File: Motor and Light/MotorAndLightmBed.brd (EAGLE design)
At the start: 100 x 110.5 mm, 136 parts, among them J6 6_PIN_SERIAL_CABLEPTH, Q1 BSS84, Q3 BC846ASMD, Q4 220mA/50V/3.5Ω, Q5 220mA/50V/3.5Ω, Q6 220mA/50V/3.5Ω, Q7 220mA/50V/3.5Ω, U1 9DoF IMU, U2 LPC1768FBD100, X1 2510-, X2 2510-, X3 C-GRID-05-15-91, X4 C-GRID-05-15-91, X5 C-GRID-02-70553, X6 SI-50170, Y1 32.768kHz, Y2 OSCILLATORSMD-5X3-50MHz, Y3 OSCILLATORSMD-5X3-12MHz

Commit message: Updated Board Design
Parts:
- removed U$3: V_REG_LD1117VXX, SparkFun-IC-Power:78XXL
- added CR1: LD1117S33TR, LD1117:SOT-223
- moved R32 194.9 mm to (79.5, 6.50), turned to 270 degrees
- moved J6 177.3 mm to (83.0, 24.5)
- moved R33 123.5 mm to (82.5, 21.0)
- moved C3 123.4 mm to (43.5, 49.0), turned to 270 degrees
- moved R54 122.1 mm to (59.5, 50.0)
- moved C10 116.2 mm to (11.0, 43.0), turned to 180 degrees
- moved Y2 114.9 mm to (47.6, 5.47)
- moved R31 112.0 mm to (11.0, 47.5)
- moved R30 109.6 mm to (11.0, 45.0)
- moved R1 104.5 mm to (8.18, 39.4)
- moved R53 102.5 mm to (48.0, 65.0)
- moved Y3 97.6 mm to (37.5, 49.0)
- moved R56 94.7 mm to (29.5, 68.5)
- moved R52 75.1 mm to (16.0, 53.8), turned to 90 degrees
- moved R51 69.8 mm to (16.0, 57.6), turned to 90 degrees
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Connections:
- new net USB_D+: C10.1, R1.2, R30.2, U2.29
- new net USB_D-: C11.1, R31.2, U2.30
- net +3V3: now also CR1.2; no longer U$3.GND
- net +5V: now also CR1.3; no longer U$3.OUT
- net GND: now also CR1.1; no longer U$3.IN
- net LEA3: now also U2.52; no longer U2.77
- net LPC_D+: no longer C10.1, R1.2, R30.2, U2.29
- net LPC_D-: no longer C11.1, R31.2, U2.30
- net REA3: now also U2.51; no longer U2.79
- net REB3: now also U2.77; no longer U2.78
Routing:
- net +3V3: track 89.9 -> 410.1 mm, vias 4 -> 19
- net +5V: track 49.9 -> 177.7 mm, vias 3 -> 6
- net GND: track 160.4 -> 270.0 mm, vias 7 -> 19
- net +12V: track 0.00 -> 91.6 mm, vias 0 -> 1
- net LED_LINK: track 0.00 -> 82.0 mm, vias 0 -> 2
- net TGT_RXD: track 0.00 -> 75.7 mm, vias 0 -> 1
- net LED_SPEED: track 0.00 -> 75.6 mm, vias 0 -> 2
- net ETH_RST: track 0.00 -> 75.4 mm, vias 0 -> 2
- net 50MHZ: track 0.00 -> 74.4 mm, vias 0 -> 6
- net TGT_TXD: track 0.00 -> 73.2 mm, vias 0 -> 1
- net VDDA: track 0.00 -> 61.5 mm, vias 0 -> 2
- net N$11: track 0.00 -> 57.6 mm, vias 0 -> 4
- net TGT_SCON: track 0.00 -> 56.5 mm, vias 0 -> 2
- net TGT_P1.17: track 0.00 -> 53.1 mm, vias 0 -> 2
- net TGT_P1.16: track 0.00 -> 50.5 mm, vias 0 -> 2
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- added copper zone on layer 16, net GND
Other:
- board size 100 x 110.5 mm -> 100 x 80 mm

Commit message: First Version of Board file
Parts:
- moved R55 124.8 mm to (65.3, 72.5)
- moved C1 122.5 mm to (50.0, 48.5), turned to 180 degrees
- moved C2 119.9 mm to (43.5, 48.5)
- moved C28 118.6 mm to (28.5, 26.5), turned to 180 degrees
- moved R29 116.7 mm to (22.5, 44.5)
- moved C26 115.1 mm to (32.0, 26.5)
- moved R57 113.6 mm to (46.2, 72.5)
- moved C29 104.4 mm to (13.1, 34.8), turned to 90 degrees
- moved Y1 93.9 mm to (45.0, 51.5)
- moved C24 91.6 mm to (13.0, 30.0), turned to 270 degrees
- moved C27 79.4 mm to (3.50, 55.5), turned to 180 degrees
- moved S1 76.6 mm to (31.0, 30.5)
- moved C16 74.7 mm to (18.5, 36.0)
- moved C15 70.6 mm to (18.5, 38.0)
- moved R15 65.6 mm to (13.0, 73.0), turned to 90 degrees
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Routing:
- net +3V3: track 410.1 -> 57.1 mm, vias 19 -> 8
- net NRESET: track 0.00 -> 114.1 mm, vias 0 -> 5
- net TDI: track 0.00 -> 90.6 mm
- net TCLK: track 0.00 -> 77.9 mm, vias 0 -> 2
- net 2S1: track 0.00 -> 70.7 mm, vias 0 -> 4
- net RTCK: track 0.00 -> 69.7 mm
- net TDO: track 0.00 -> 67.6 mm, vias 0 -> 4
- net TMS: track 0.00 -> 60.2 mm, vias 0 -> 2
- net BATTIN: track 11.9 -> 57.4 mm, vias 1 -> 2
- net 1S3: track 0.00 -> 44.2 mm, vias 0 -> 2
- net GND: track 270.0 -> 312.4 mm, vias 19 -> 25
- net 1S1: track 0.00 -> 39.4 mm, vias 0 -> 4
- net 1S2: track 0.00 -> 34.6 mm, vias 0 -> 2
- net 1S3O: track 0.00 -> 34.5 mm, vias 0 -> 1
- net 2S3O: track 0.00 -> 34.1 mm
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- added copper zone on layer 1, net +3V3

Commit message: Minor Changes to V1
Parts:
- moved R2 16.0 mm to (22.5, 19.0), turned to 90 degrees
- moved R4 14.7 mm to (5.50, 17.0), turned to 270 degrees
- moved R7 13.1 mm to (5.50, 12.5), turned to 90 degrees
- moved R5 12.5 mm to (22.5, 15.0), turned to 90 degrees
- moved R11 11.5 mm to (36.5, 16.0), turned to 270 degrees
- moved R8 9.55 mm to (34.5, 16.0), turned to 90 degrees
- moved X2 8.75 mm to (11.0, 5.50), turned to 0 degrees
- moved OK1 7.83 mm to (28.5, 16.0), turned to 270 degrees
- moved R9 6.80 mm to (19.0, 14.5), turned to 270 degrees
- moved OK3 6.50 mm to (10.5, 14.0), turned to 270 degrees
- moved X1 5.59 mm to (32.5, 8.00), turned to 0 degrees
- moved R10 4.03 mm to (16.5, 14.5), turned to 90 degrees
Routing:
- net RDISABLE: track 58.5 -> 0.00 mm, vias 3 -> 0
- net RDIR: track 49.4 -> 0.00 mm, vias 2 -> 0
- net RSPEED: track 44.9 -> 0.00 mm, vias 2 -> 0
- net LVCC: track 26.8 -> 8.17 mm
- net LSPEED: track 56.1 -> 39.0 mm
- net LBLI: track 16.6 -> 1.76 mm
- net LDIR: track 50.9 -> 39.4 mm
- net LGND: track 15.3 -> 4.23 mm
- net LDISABLE: track 56.6 -> 47.6 mm
- net LALI: track 12.8 -> 3.89 mm, vias 1 -> 0
- net GND: track 312.4 -> 309.6 mm, vias 25 -> 24
- net RVCC: track 26.8 -> 28.1 mm
- net RBLI: track 14.9 -> 13.8 mm
- net VDDA: track 60.9 -> 61.9 mm
- net N$41: track 17.4 -> 18.4 mm
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- removed copper zone on layer 1, net +3V3
- removed copper zone on layer 16, net GND

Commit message: update
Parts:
- added R3, R6: 2700, SparkFun-Resistors:0603
- added T10: (no value), transistor:TO220V
- moved R2 3.16 mm to (23.5, 16.0), turned to 270 degrees
- moved R5 2.69 mm to (23.5, 12.5)
- moved X1 2.50 mm to (32.5, 5.50)
- moved OK1 2.06 mm to (29.0, 14.0)
- moved R11 2.06 mm to (37.0, 14.0)
- moved R8 2.06 mm to (35.0, 14.0)
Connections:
- new net N$24: J4.1, R6.1, T10.2
- net +12V: now also R6.2
- net ESTOP: now also R3.2, U2.46
- net GND: now also R3.1, T10.3
- net SLIGHT: now also T10.1, U2.47; no longer J4.1
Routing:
- net LED_LINK: track 82.0 -> 0.00 mm, vias 2 -> 0
- net LED_SPEED: track 75.6 -> 0.00 mm, vias 2 -> 0
- net ETH_RST: track 75.4 -> 0.00 mm, vias 2 -> 0
- net ETH_OSC_EN: track 49.6 -> 0.00 mm, vias 2 -> 0
- net LSPEED: track 39.0 -> 0.00 mm
- net LDISABLE: track 47.6 -> 23.7 mm, vias 1 -> 0
- net LDIR: track 39.4 -> 24.2 mm
- net GND: track 309.6 -> 300.7 mm
- net LVCC: track 8.17 -> 0.00 mm
- net N$1: track 4.56 -> 0.00 mm
- net LGND: track 4.23 -> 0.00 mm
- net LALI: track 3.89 -> 0.00 mm
- net N$9: track 3.48 -> 0.00 mm
- net LBLI: track 1.76 -> 0.00 mm
- net RBLI: track 13.8 -> 14.6 mm
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
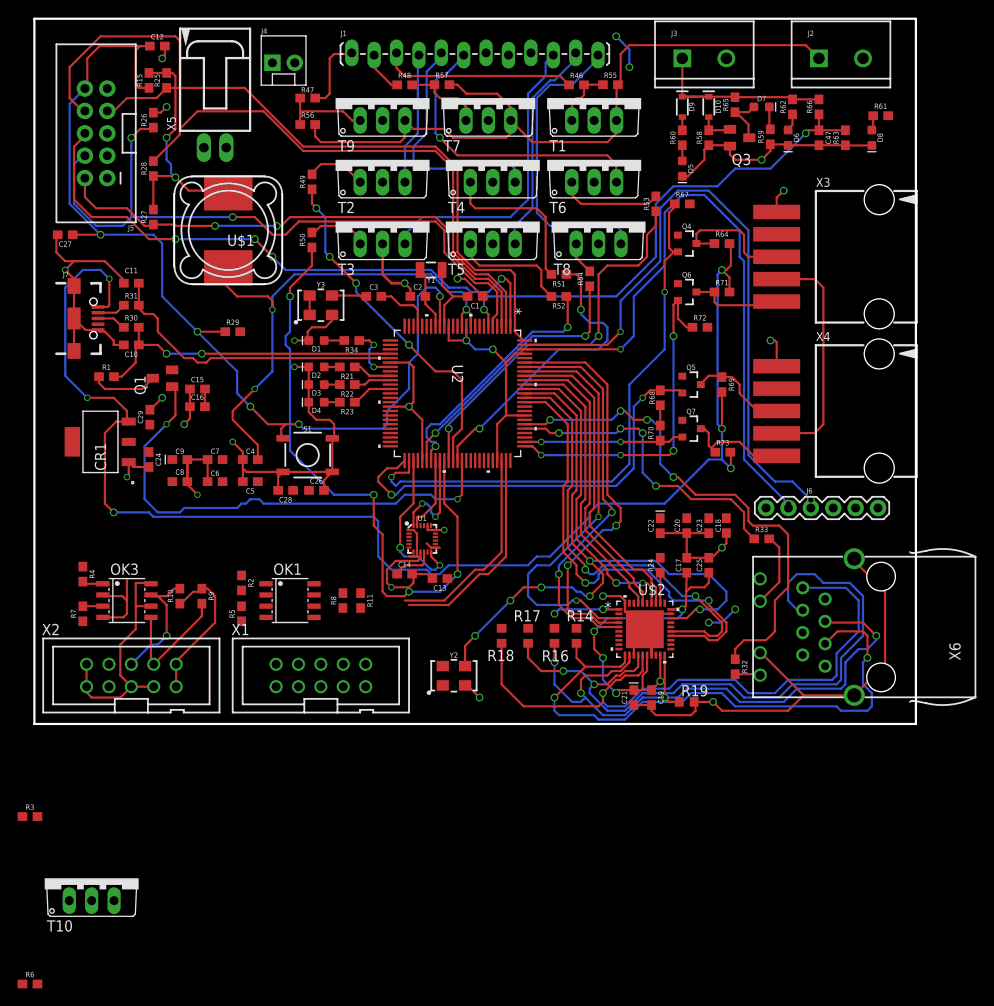
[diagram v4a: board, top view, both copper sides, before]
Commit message: Finalized
Final Submission before design review. IMU problem remain unresolved.
Micro-usb-b addressed.
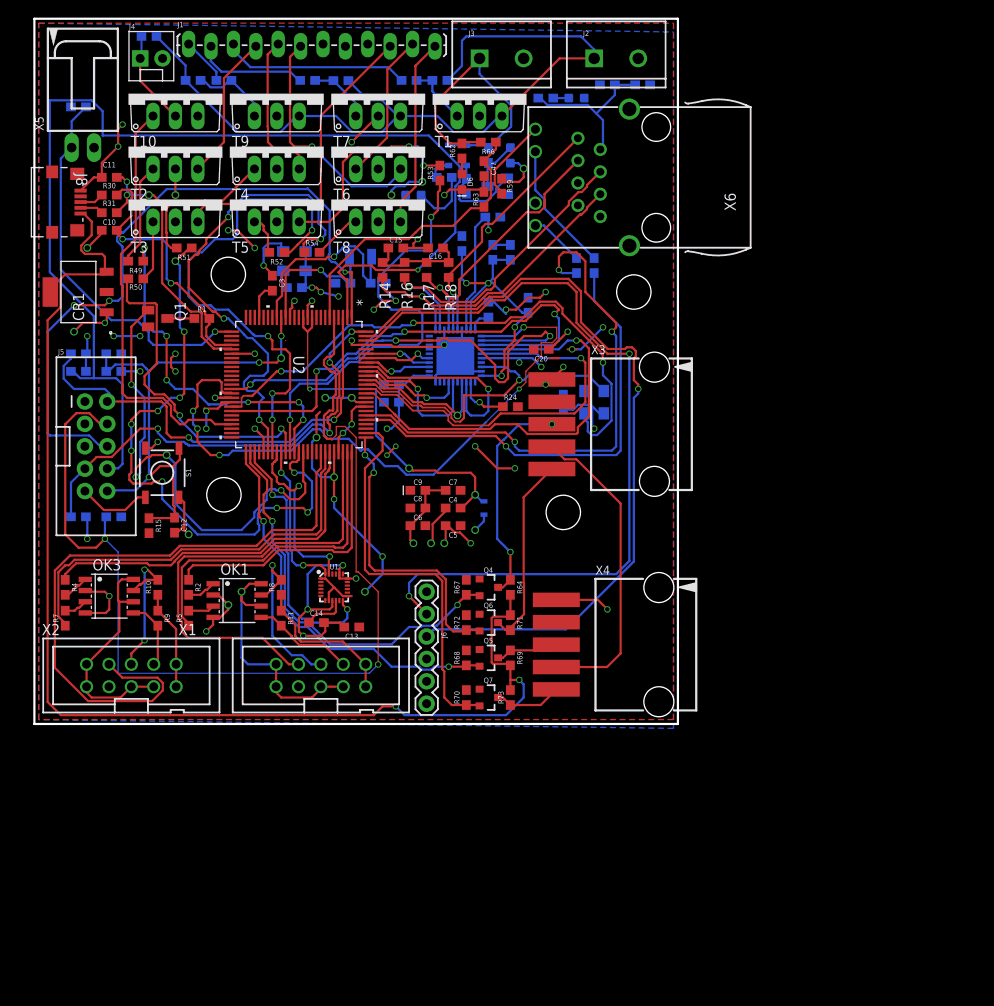
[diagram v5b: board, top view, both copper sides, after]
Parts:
- removed D1, D2, D3, D4: BLUE, SparkFun-LED:LED-0603
- removed J7: (no value), SparkFun-Connectors:USB-B-MICRO-SMD
- removed R21, R22, R23, R34: 200, SparkFun-Resistors:0603
- removed U$1: 10uH, inductor-coilcraft:MSS1260
- added J8: 1981568-1, DigiKey:CONN_1981568-1
- added L1: 10uH, DigiKey:IND_1608
- added U$3, U$4, U$5, U$6: (no value), temp:STANDOFF-HOLE
- moved R6 108.3 mm to (13.0, 78.0), flipped to the bottom, turned to 180 degrees
- moved T10 89.5 mm to (16.0, 71.5)
- moved R3 80.7 mm to (5.00, 70.0), flipped to the bottom, turned to 180 degrees
- moved C29 67.4 mm to (69.0, 72.5), flipped to the bottom, turned to 180 degrees
- moved C28 58.7 mm to (65.0, 72.5), flipped to the bottom, turned to 0 degrees
- moved X6 57.0 mm to (67.5, 62.0)
- moved C12 54.4 mm to (15.9, 22.6), turned to 270 degrees
- moved C19 53.0 mm to (54.0, 53.5), flipped to the bottom, turned to 90 degrees
- moved C21 53.0 mm to (52.0, 53.5), flipped to the bottom, turned to 270 degrees
- moved R15 50.5 mm to (13.0, 22.5), turned to 270 degrees
- moved R25 50.5 mm to (5.00, 23.5), flipped to the bottom, turned to 180 degrees
- moved R67 49.9 mm to (49.0, 15.5), turned to 90 degrees
- moved R19 49.9 mm to (51.5, 47.0), flipped to the bottom, turned to 90 degrees
- moved R32 48.9 mm to (61.5, 52.0), flipped to the bottom, turned to 90 degrees
- moved C24 47.4 mm to (60.0, 36.5), flipped to the bottom, turned to 90 degrees
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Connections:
- removed net LED-1: R34.1, U2.32
- removed net LED-2: R21.1, U2.34
- removed net LED-3: R22.1, U2.35
- removed net LED-4: R23.1, U2.37
- removed net N$17: D1.A, R34.2
- removed net N$18: D2.A, R21.2
- removed net N$19: D3.A, R22.2
- removed net N$20: D4.A, R23.2
- net +3V3: now also L1.2; no longer U$1.P$2
- net +5V: now also J8.1; no longer J7.VBUS
- net ESTOP: now also U2.26; no longer U2.46
- net GND: now also J8.5; no longer D1.C, D2.C, D3.C, D4.C, J7.GND, J7.SHIELD1, J7.SHIELD2, J7.SHIELD3
- net LPC_D+: now also J8.3; no longer J7.D+
- net LPC_D-: now also J8.2; no longer J7.D-
- net VDDA: now also L1.1; no longer U$1.P$1
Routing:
- net +3V3: track 57.1 -> 150.8 mm, vias 8 -> 27
- net GND: track 300.7 -> 212.1 mm, vias 24 -> 47
- net LED_SPEED: track 0.00 -> 75.5 mm, vias 0 -> 5
- net RDISABLE: track 0.00 -> 73.5 mm
- net ETH_OSC_EN: track 0.00 -> 64.3 mm, vias 0 -> 3
- net ETH_RST: track 0.00 -> 57.6 mm, vias 0 -> 3
- net NRESET: track 114.1 -> 59.6 mm, vias 5 -> 4
- net LED_LINK: track 0.00 -> 53.8 mm, vias 0 -> 3
- net SLIGHT: track 0.00 -> 47.9 mm
- net RDIR: track 0.00 -> 47.2 mm
- net TD+: track 72.6 -> 28.5 mm
- net ESTOP: track 0.00 -> 43.7 mm, vias 0 -> 1
- net TD-: track 75.3 -> 31.8 mm, vias 2 -> 1
- net TCLK: track 77.9 -> 120.6 mm
- net RSPEED: track 0.00 -> 41.6 mm
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- added copper zone on layer 1, net +3V3
- added copper zone on layer 16, net GND
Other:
- board size 100 x 80 mm -> 73 x 80 mm

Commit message: Bad Update After Review
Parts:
- removed D8: (no value), SparkFun-LED:LED-0603
- removed J8: 1981568-1, DigiKey:CONN_1981568-1
- removed OK3: MOCD208M, optocoupler:SOIC08-FAIRCHILD
- removed Q7: 220mA/50V/3.5Ω, SparkFun-DiscreteSemi:SOT23-3
- removed R57, R58: 200, SparkFun-Resistors:0603
- removed R60, R61, R65: 2700, SparkFun-Resistors:0603
- removed R63: 536, SparkFun-Resistors:0603
- removed R68, R69, R70, R73: 10k, SparkFun-Resistors:0603
- added D2: (no value), SparkFun-LED:LED-0603
- added J7: (no value), SparkFun-Connectors:SCREWTERMINAL-5MM-2
- added OK2: MOCD208M, optocoupler:SOIC08-FAIRCHILD
- added Q2: BC846ASMD, transistor-npn:SOT23
- added R12, R13: 49.9, rcl:R0603
- added R20: 10k, SparkFun-Resistors:0603
- added R21: 4.87k, rcl:R0603
- added R22: 100k, SparkFun-Resistors:0603
- added R23: 150, SparkFun-Resistors:0603
- added R36, R42: 2700, SparkFun-Resistors:0603
- added R37, R38: 200, SparkFun-Resistors:0603
- C1, C10, C11, C2: value 18pF -> 0.1uF
- C12: value 1nF -> 0.1uF
- C13, C15: value 0.1uF -> 10uF; device SparkFun-Capacitors:0603 -> SparkFun-Capacitors:0603-POLAR
- C22, C9: value 10uF -> 0.1uF; device SparkFun-Capacitors:0603-POLAR -> SparkFun-Capacitors:0603
- C3: value 100pF -> 18pF
- C4, C5, C6: value 0.1uF -> 18pF
- C7: value 0.1uF -> 100pF
- C8: value 0.1uF -> 1000pF
- J1: value (none) -> 1981568-1; device SparkFun-Connectors:1X12_LOCK_LONGPADS -> DigiKey:CONN_1981568-1
- J2: device SparkFun-Connectors:SCREWTERMINAL-5MM-2 -> SparkFun-Connectors:2X5-SHROUDED
- J3: value (none) -> 6_PIN_SERIAL_CABLEPTH; device SparkFun-Connectors:SCREWTERMINAL-5MM-2 -> SparkFun-Connectors:FTDI_BASIC
- J4: device SparkFun-Retired:MOLEX-1X2 -> SparkFun-Connectors:1X12_LOCK_LONGPADS
- J5: device SparkFun-Connectors:2X5-SHROUDED -> SparkFun-Retired:MOLEX-1X2
- J6: value 6_PIN_SERIAL_CABLEPTH -> (none); device SparkFun-Connectors:FTDI_BASIC -> SparkFun-Connectors:SCREWTERMINAL-5MM-2
- Q3: value BC846ASMD -> 220mA/50V/3.5Ω; device transistor-npn:SOT23 -> SparkFun-DiscreteSemi:SOT23-3
- R1: value 1.5k -> 33
- R10, R9: value 10k -> 1k
- R15: value 47k -> 49.9; device SparkFun-Resistors:0603 -> rcl:R0603
- R16, R17, R18: value 49.9 -> 10k; device rcl:R0603 -> SparkFun-Resistors:0603
- R19: value 4.87k -> 10k; device rcl:R0603 -> SparkFun-Resistors:0603
- R2: value 1k -> 33
- R24: value 2.2k -> 150
- R25: value 10k -> 2.2k
- R26, R27: value 10k -> 2700
- R28: value 10k -> 200
- R29: value 100k -> 200
- R3: value 2700 -> 1.5k
- R30: value 33 -> 2700
- R31: value 33 -> 200
- R32: value 150 -> 200
- R33: value 150 -> 2700
- R46: value 2700 -> 536
- R47, R48: value 2700 -> 200
- R49, R52: value 200 -> 2700
- R50, R51, R54, R55: value 200 -> 10k
- R6: value 2700 -> 47k
- R7: value 1k -> 10k
- X3: value C-GRID-05-15-91 -> SI-50170; device con-molex:15-91-05 -> con-stewart:SI-50170
- X5: value C-GRID-02-70553 -> C-GRID-05-15-91; device con-molex:70553-02 -> con-molex:15-91-05
- X6: value SI-50170 -> C-GRID-02-70553; device con-stewart:SI-50170 -> con-molex:70553-02
- Y2: value OSCILLATORSMD-5X3-50MHz -> OSCILLATORSMD-5X3-12MHz
- Y3: value OSCILLATORSMD-5X3-12MHz -> OSCILLATORSMD-5X3-50MHz
- moved X5 90.5 mm to (69.5, 9.00), turned to 270 degrees
- moved J2 71.6 mm to (7.00, 31.5)
- moved R55 70.5 mm to (54.0, 3.00), flipped to the top, turned to 90 degrees
- moved J6 63.4 mm to (63.5, 75.5), turned to 0 degrees
- moved X6 63.0 mm to (5.50, 73.0), turned to 0 degrees
- moved J3 60.8 mm to (44.5, 15.0), turned to 270 degrees
- moved R51 60.2 mm to (49.0, 3.00), turned to 90 degrees
- moved R50 57.1 mm to (49.0, 7.50), turned to 90 degrees
- moved R6 55.5 mm to (13.0, 22.5), flipped to the top, turned to 270 degrees
- moved R26 53.7 mm to (46.5, 62.0), turned to 0 degrees
- moved C6 52.8 mm to (8.50, 62.0)
- moved C27 51.3 mm to (60.0, 36.5), turned to 90 degrees
- moved R54 51.2 mm to (54.0, 7.50), turned to 270 degrees
- moved R25 50.6 mm to (54.0, 36.0), flipped to the top, turned to 0 degrees
- moved R17 49.9 mm to (14.0, 12.0)
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- renumbered C47 to C30, D10 to D3, D7 to D4, D9 to D1, R56 to R41, R59 to R34, R62 to R35, R64 to R43, R66 to R45, R67 to R39, R71 to R44, R72 to R40, U$2 to MU1
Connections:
- removed net TRST: U2.4
- net +12V: now also J6.1, R30.2, R32.2, R53.2, T2.3, T5.3, T8.3; no longer J2.1, R55.2, R57.2, R6.2, T1.3, T7.3, T9.3
- net +24V: now also J7.1, R33.2; no longer J3.1, R65.2
- net +3V3: now also C1.1, C10.2, C11.1, C15.+, C17.2, C19.1, C21.+, C22.1, C23.1, C25.1, C27.1, C29.2, C9.2, Q3.1, R11.2, R12.1, R13.2, R20.1, R22.2, R50.2, R51.2, R52.2, R6.2, X3.2, X3.5, Y2.1; no longer C13.1, C15.2, C16.2, C20.2, C22.+, C23.2, C28.1, C29.1, C5.1, C6.1, C7.1, C8.1, C9.+, Q7.1, R16.2, R17.1, R24.2, R27.2, R28.1, R29.2, R61.2, R68.2, R70.2, X6.2, X6.5, Y3.1
- net +5V: now also J1.1, R54.2, R55.2; no longer J8.1, R69.2, R73.2
- net 12MHZ: now also C7.1, Y2.3; no longer C3.1, Y3.3
- net 1S1: now also R28.1; no longer R49.1
- net 1S1O: now also J4.4, T3.3; no longer J1.4, T2.3
- net 1S2: now also R37.1; no longer R51.1
- net 1S2O: now also J4.5, T6.3; no longer J1.5, T4.3
- net 1S3: now also R47.1; no longer R53.1
- net 1S3O: now also J4.6, T9.3; no longer J1.6, T6.3
- net 2S1: now also R29.1; no longer R50.1
- net 2S1O: now also J4.10, T4.3; no longer J1.10, T3.3
- net 2S2: now also R38.1; no longer R52.1
- net 2S2O: now also J4.11, T7.3; no longer J1.11, T5.3
- net 2S3: now also R48.1; no longer R54.1
- net 2S3O: now also J4.12, T10.3; no longer J1.12, T8.3
- net 50MHZ: now also Y3.3; no longer Y2.3
- net BATTIN: now also R46.2; no longer R63.2
- net BLUE: now also J4.1, R36.1; no longer J1.1, R47.1
- net ESTOP: now also R42.2, X6.1, X6.2; no longer R3.2, X5.1
- net ETH_LED1: now also R23.2, X3.A1; no longer R32.2, X6.A1
- net ETH_LED2: now also R24.2, X3.A2; no longer R33.2, X6.A2
- net ETH_OSC_EN: now also Y3.1; no longer Y2.1
- net GND: now also C1.2, C10.1, C13.-, C14.1, C15.-, C16.2, C2.2, C20.2, C22.2, C23.2, C29.1, C3.2, C4.1, C5.1, C9.1, D2.C, J1.5, J2.3, J2.5, J2.9, J3.GND, J6.2, J7.2, OK2.2, OK2.4, Q2.2, R21.2, R31.1, R42.1, R46.1, T1.3, T10.2, X3.C1, X3.C2, X3.S1, X3.S2, X5.1; no longer C1.1, C10.2, C13.2, C14.2, C15.1, C16.1, C2.1, C20.1, C22.-, C23.1, C29.2, C4.2, C5.2, C7.2, C9.-, D8.C, J2.2, J3.2, J5.3, J5.5, J5.9, J6.GND, J8.5, OK3.2, OK3.4, Q3.2, R26.2, R3.1, R58.1, R63.1, S1.2, S1.3, T1.2, T10.3, X3.1, X6.C1, X6.C2, X6.S1, X6.S2
- net GREEN: now also J4.2, R49.1; no longer J1.2, R48.1
- net LALI: now also R7.2; no longer R8.2
- net LBLI: now also R16.2; no longer R11.2
- net LDIR: now also R9.1; no longer R5.1
- net LEA: now also Q3.3, X4.3; no longer Q4.3, X3.3
- net LEA3: now also Q3.2; no longer Q4.2
- net LEB: now also Q4.3, X4.5; no longer Q6.3, X3.5
- net LEB3: now also Q4.2; no longer Q6.2
- net LGND: now also R16.1, R7.1; no longer R11.1, R8.1
- net LPC_D+: now also J1.3, R1.1; no longer J8.3, R30.1
- net LPC_D-: now also J1.2, R2.1; no longer J8.2, R31.1
- net LSPEED: now also R4.1; no longer R2.1
- net N$1: now also R4.2; no longer R2.2
- net N$10: now also C7.2; no longer C3.2
- net N$11: now also R23.1; no longer R32.1
- net N$13: now also C2.1; no longer C14.1
- net N$14: now also R21.1; no longer R19.1
- net N$15: now also R24.1; no longer R33.1
- net N$16: now also R25.1; no longer R24.1
- net N$2: now also C4.2; no longer C1.2
- net N$24: now also J5.1, J5.2, R30.1, T1.2; no longer J4.1, R6.1, T10.2
- net N$3: now also C5.2; no longer C2.2
- net N$34: now also R27.2, R32.1, T2.1; no longer R46.2, R55.1, T1.1
- net N$36: now also R36.2, T5.1; no longer R47.2, T9.1
- net N$38: now also R49.2, R53.1, T8.1; no longer R48.2, R57.1, T7.1
- net N$4: now also R3.1; no longer R1.1
- net N$40: now also R47.2, T9.1; no longer R53.2, T6.1
- net N$41: now also R37.2, T6.1; no longer R51.2, T4.1
- net N$42: now also R28.2, T3.1; no longer R49.2, T2.1
- net N$43: now also R29.2, T4.1; no longer R50.2, T3.1
- net N$44: now also R38.2, T7.1; no longer R52.2, T5.1
- net N$45: now also R48.2, T10.1; no longer R54.2, T8.1
- net N$46: now also R26.2; no longer R60.2
- net N$47: now also D2.A, R26.1; no longer D5.A, R60.1
- net N$49: now also Q2.1, R31.2; no longer Q3.1, R58.2
- net N$50: now also D5.A; no longer D6.A
- net N$51: now also Q2.3, R33.1; no longer Q3.3, R65.1
- net N$54: now also D6.A, R52.1; no longer D8.A, R61.1
- net N$6: now also OK2.1, R5.2; no longer OK3.1, R4.2
- net N$7: now also OK2.3, R10.2; no longer OK3.3, R7.2
- net N$9: now also R9.2; no longer R5.2
- net NRESET: now also C16.1, C8.1, J2.10, R22.1, R6.1; no longer C12.1, C27.1, J5.10, R15.1, R29.1
- net PFBOUT: now also C12.1, C13.+, C14.2, C28.1; no longer C17.2, C19.1, C21.+, C25.1
- net RALI: now also OK2.7, R8.2; no longer OK3.7, R10.2
- net RBLI: now also OK2.5, R17.2; no longer OK3.5, R9.2
- net RD+: now also R13.1, X3.4; no longer R16.1, X6.4
- net RD-: now also R12.2, X3.6; no longer R14.2, X6.6
- net RDIR: now also R10.1; no longer R7.1
- net REA: now also R54.1, X5.3; no longer R69.1, X4.3
- net REA3: now also R50.1; no longer R68.1
- net REB: now also Q6.3, R55.1, X5.5; no longer Q7.3, R73.1, X4.5
- net REB3: now also Q6.2, R51.1; no longer Q7.2, R70.1
- net RED: now also J4.3, R27.1; no longer J1.3, R46.1
- net RGND: now also R17.1, R8.1; no longer R10.1, R9.1
- net RSPEED: now also R5.1; no longer R4.1
- net RTCK: now also J2.7, R11.1; no longer J5.7, R25.1
- net RVCC: now also OK2.6, OK2.8; no longer OK3.6, OK3.8
- net SLIGHT: now also T1.1; no longer T10.1
- net TCLK: now also J2.4, R19.1; no longer J5.4, R26.1
- net TD+: now also R15.1, X3.1; no longer R18.1, X6.1
- net TD-: now also R14.2, X3.3; no longer R17.2, X6.3
- net TDI: now also J2.8, R20.2; no longer J5.8, R28.2
- net TDO: now also J2.6; no longer J5.6
- net TGT_RXD: now also J3.TXO; no longer J6.TXO
- net TGT_TXD: now also J3.RXI; no longer J6.RXI
- net TMS: now also J2.2, R18.1; no longer J5.2, R27.1
- net USB_D+: now also C3.1, R3.2; no longer C10.1, R30.2
- net USB_D-: now also C6.1, R2.2; no longer C11.1, R31.2
- net VCC: now also X5.4; no longer X3.4
- net VDDA: now also C20.1; no longer C4.1
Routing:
- net GND: track 212.1 -> 188.4 mm, vias 47 -> 44
- net +3V3: track 150.8 -> 142.5 mm, vias 27 -> 25
- net N$24: track 10.8 -> 13.3 mm
- net ESTOP: track 43.7 -> 46.3 mm
- net VDDA: track 41.9 -> 44.4 mm, vias 3 -> 2
- net TDI: track 131.2 -> 130.1 mm
- net LEB: track 23.3 -> 24.4 mm
- net RALI: track 16.6 -> 15.8 mm
- net RVCC: track 26.0 -> 26.6 mm
- net LALI: track 19.9 -> 19.4 mm
- net TCLK: track 120.6 -> 120.0 mm
- net VCC: track 35.4 -> 35.9 mm

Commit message: Board Last Updates
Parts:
- added U$13: (no value), RoboJackets-Aesthetics:ROBOBUZZ_1.0X
- D2: value (none) -> RED
- D4: value (none) -> GREEN
- D5: value (none) -> BLUE
- D6: value (none) -> WHITE
- J2: value (none) -> Programming Port
- J4: value (none) -> Under Glow
- J5: value (none) -> Safety Light
- J6: value (none) -> 12V
- J7: value (none) -> 24V
- S1: value (none) -> Momentary Switch 5.2mm
- T1, T10, T2, T3, T4, T5, T6, T7, T8, T9: value (none) -> TIP41A
- moved X6 5.50 mm to (5.50, 78.5)
- moved R42 3.54 mm to (5.50, 66.5), flipped to the top
- renumbered MU1 to U3
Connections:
- net LVCC renamed L+12V
- net RVCC renamed R+12V
- removed net LVBATT: X1.3
- removed net RVBATT: X2.3
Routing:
- net ESTOP: track 46.3 -> 51.8 mm
- net TDI: track 130.1 -> 135.6 mm
- net +3V3: track 142.5 -> 145.2 mm, vias 25 -> 26
- net R+12V: track 26.6 -> 24.9 mm
- net GND: track 188.4 -> 190.0 mm, vias 44 -> 45
